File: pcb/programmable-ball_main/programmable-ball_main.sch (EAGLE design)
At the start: 4 parts, among them J1 12402012E212A, U1 MDBT50Q-1MV2

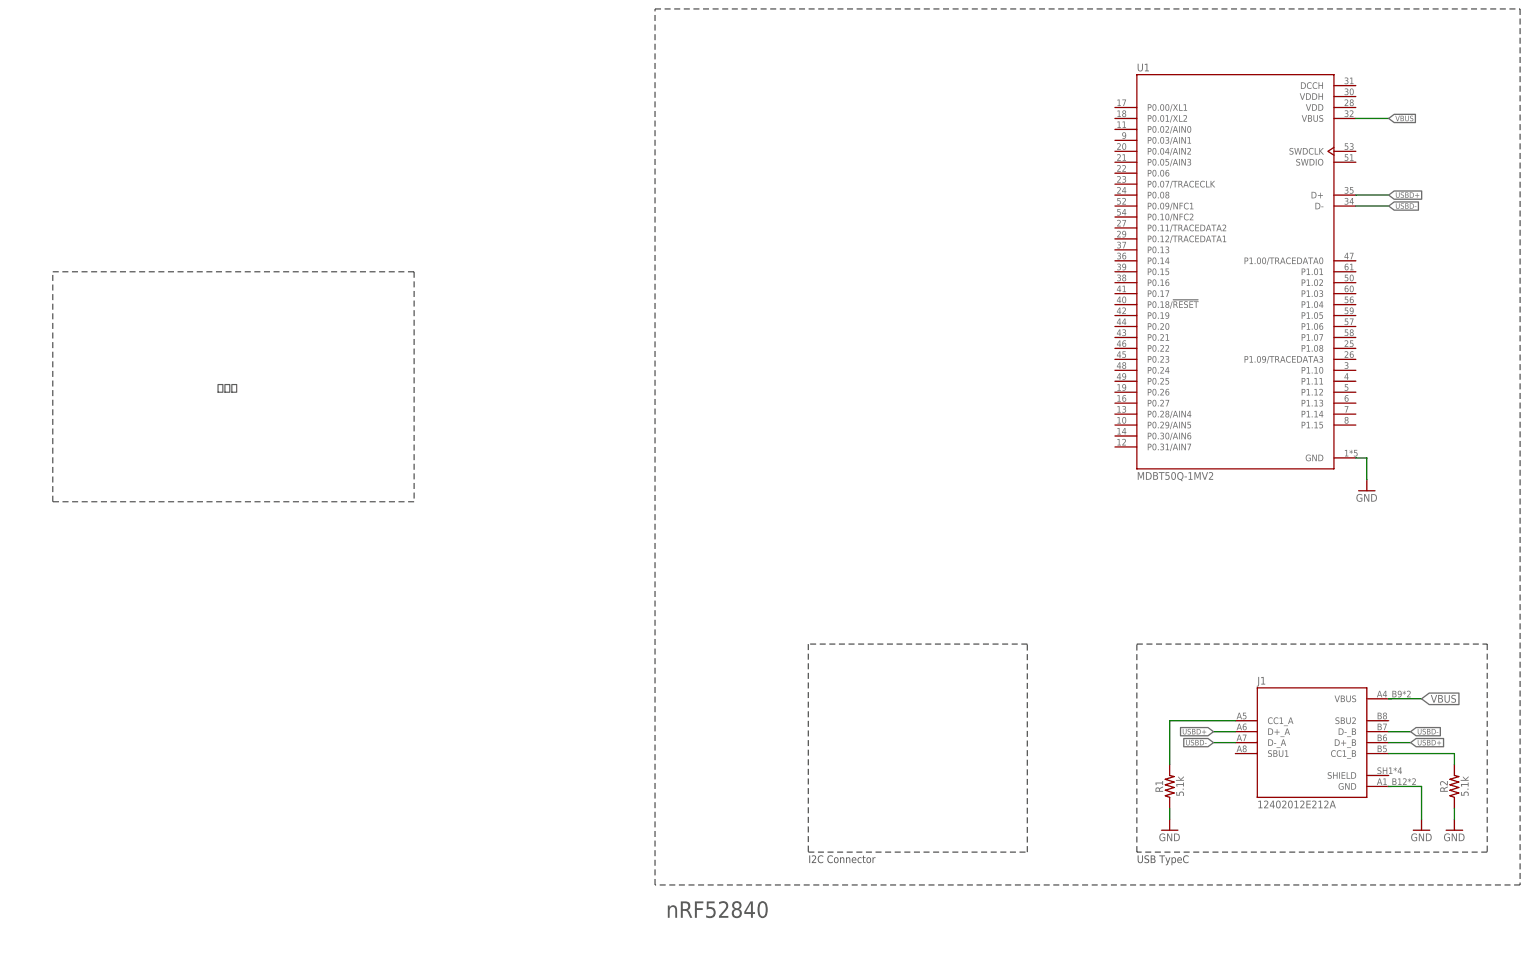
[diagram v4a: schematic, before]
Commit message: スイッチを追加 #4
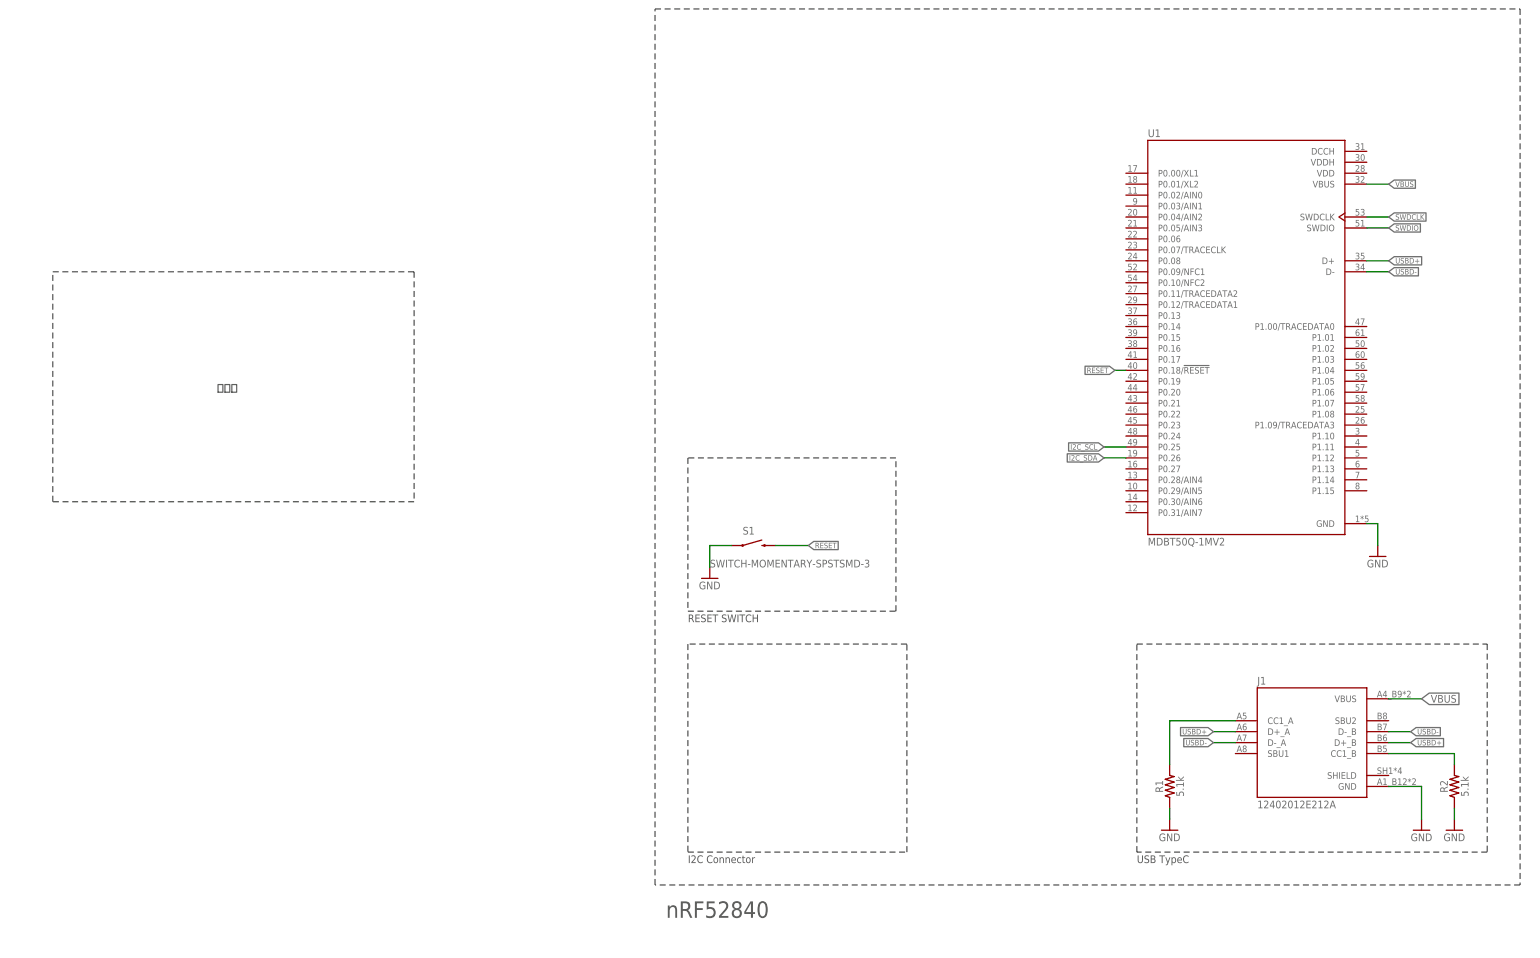
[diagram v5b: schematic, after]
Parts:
- added S1: SWITCH-MOMENTARY-SPSTSMD-3, SparkFun-Retired:SWITCH-MOMENTARY-SPSTSMD-3
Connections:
- new net I2C_SCL: U1.P0.25
- new net I2C_SDA: U1.P0.26
- new net RESET: S1.2, U1.P0.18/!RESET
- new net SWDCLK: U1.SWDCLK
- new net SWDIO: U1.SWDIO
- net GND: now also S1.1
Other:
- note added: "RESET SWITCH"
- moved on the sheet: U1
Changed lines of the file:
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@@
 <part name="R1" library="SparkFun-Resistors" deviceset="5.1KOHM" device="-0402T-1/16W-1%" value="5.1k"/>
 <part name="R2" library="SparkFun-Resistors" deviceset="5.1KOHM" device="-0402T-1/16W-1%" value="5.1k"/>
+<part name="S1" library="SparkFun-Retired" deviceset="SWITCH-MOMENTARY-SPST" device="SMD-3"/>
+<part name="GND5" library="supply1" library_urn="urn:adsk.eagle:library:371" deviceset="GND" device=""/>
 </parts>
 <sheets>
@@
 <wire x1="276.86" y1="50.8" x2="276.86" y2="99.06" width="0.1524" layer="97" style="shortdash"/>
 <text x="276.86" y="48.26" size="1.778" layer="97">USB TypeC</text>
-<wire x1="200.66" y1="99.06" x2="200.66" y2="50.8" width="0.1524" layer="97" style="shortdash"/>
-<wire x1="200.66" y1="50.8" x2="251.46" y2="50.8" width="0.1524" layer="97" style="shortdash"/>
-<wire x1="251.46" y1="50.8" x2="251.46" y2="99.06" width="0.1524" layer="97" style="shortdash"/>
-<wire x1="251.46" y1="99.06" x2="200.66" y2="99.06" width="0.1524" layer="97" style="shortdash"/>
-<text x="200.66" y="48.26" size="1.778" layer="97">I2C Connector</text>
+<wire x1="172.72" y1="99.06" x2="172.72" y2="50.8" width="0.1524" layer="97" style="shortdash"/>
+<wire x1="172.72" y1="50.8" x2="223.52" y2="50.8" width="0.1524" layer="97" style="shortdash"/>
+<wire x1="223.52" y1="50.8" x2="223.52" y2="99.06" width="0.1524" layer="97" style="shortdash"/>
+<wire x1="223.52" y1="99.06" x2="172.72" y2="99.06" width="0.1524" layer="97" style="shortdash"/>
+<text x="172.72" y="48.26" size="1.778" layer="97">I2C Connector</text>
+<wire x1="172.72" y1="142.24" x2="172.72" y2="106.68" width="0.1524" layer="97" style="shortdash"/>
+<wire x1="172.72" y1="106.68" x2="220.98" y2="106.68" width="0.1524" layer="97" style="shortdash"/>
+<wire x1="220.98" y1="106.68" x2="220.98" y2="142.24" width="0.1524" layer="97" style="shortdash"/>
+<wire x1="220.98" y1="142.24" x2="172.72" y2="142.24" width="0.1524" layer="97" style="shortdash"/>
+<text x="172.72" y="104.14" size="1.778" layer="97">RESET SWITCH</text>
 </plain>
 <instances>
@@
 <attribute name="SHEET" x="368.3" y="4.445" size="2.54" layer="94" font="vector"/>
 </instance>
-<instance part="U1" gate="G$1" x="299.72" y="185.42" smashed="yes">
-<attribute name="NAME" x="276.86" y="231.902" size="1.778" layer="95"/>
-<attribute name="VALUE" x="276.86" y="137.16" size="1.778" layer="96"/>
-</instance>
-<instance part="GND1" gate="1" x="330.2" y="134.62" smashed="yes">
-<attribute name="VALUE" x="327.66" y="132.08" size="1.778" layer="96"/>
+<instance part="U1" gate="G$1" x="302.26" y="170.18" smashed="yes">
+<attribute name="NAME" x="279.4" y="216.662" size="1.778" layer="95"/>
+<attribute name="VALUE" x="279.4" y="121.92" size="1.778" layer="96"/>
+</instance>
+<instance part="GND1" gate="1" x="332.74" y="119.38" smashed="yes">
+<attribute name="VALUE" x="330.2" y="116.84" size="1.778" layer="96"/>
 </instance>
 <instance part="GND3" gate="1" x="342.9" y="55.88" smashed="yes">
@@
 <attribute name="NAME" x="348.996" y="66.04" size="1.778" layer="95" font="vector" rot="R90" align="bottom-center"/>
 <attribute name="VALUE" x="352.044" y="66.04" size="1.778" layer="96" font="vector" rot="R90" align="top-center"/>
+</instance>
+<instance part="S1" gate="G$1" x="187.96" y="121.92" smashed="yes">
+<attribute name="NAME" x="185.42" y="124.46" size="1.778" layer="95"/>
+<attribute name="VALUE" x="177.8" y="116.84" size="1.778" layer="96"/>
+</instance>
+<instance part="GND5" gate="1" x="177.8" y="114.3" smashed="yes">
+<attribute name="VALUE" x="175.26" y="111.76" size="1.778" layer="96"/>
 </instance>
 </instances>
@@
 <pinref part="U1" gate="G$1" pin="GND"/>
 <pinref part="GND1" gate="1" pin="GND"/>
-<wire x1="327.66" y1="142.24" x2="330.2" y2="142.24" width="0.1524" layer="91"/>
-<wire x1="330.2" y1="142.24" x2="330.2" y2="137.16" width="0.1524" layer="91"/>
+<wire x1="330.2" y1="127" x2="332.74" y2="127" width="0.1524" layer="91"/>
+<wire x1="332.74" y1="127" x2="332.74" y2="121.92" width="0.1524" layer="91"/>
 </segment>
 <segment>
@@
 <wire x1="350.52" y1="60.96" x2="350.52" y2="58.42" width="0.1524" layer="91"/>
 </segment>
+<segment>
+<pinref part="GND5" gate="1" pin="GND"/>
+<wire x1="177.8" y1="116.84" x2="177.8" y2="121.92" width="0.1524" layer="91"/>
+<pinref part="S1" gate="G$1" pin="1"/>
+<wire x1="177.8" y1="121.92" x2="182.88" y2="121.92" width="0.1524" layer="91"/>
+</segment>
 </net>
 <net name="VBUS" class="0">
 <segment>
 <pinref part="U1" gate="G$1" pin="VBUS"/>
-<wire x1="327.66" y1="220.98" x2="335.28" y2="220.98" width="0.1524" layer="91"/>
-<label x="335.28" y="220.98" size="1.27" layer="95" xref="yes"/>
+<wire x1="330.2" y1="205.74" x2="335.28" y2="205.74" width="0.1524" layer="91"/>
+<label x="335.28" y="205.74" size="1.27" layer="95" xref="yes"/>
 </segment>
 <segment>
@@
 <segment>
 <pinref part="U1" gate="G$1" pin="D+"/>
-<wire x1="327.66" y1="203.2" x2="335.28" y2="203.2" width="0.1524" layer="91"/>
-<label x="335.28" y="203.2" size="1.27" layer="95" xref="yes"/>
+<wire x1="330.2" y1="187.96" x2="335.28" y2="187.96" width="0.1524" layer="91"/>
+<label x="335.28" y="187.96" size="1.27" layer="95" xref="yes"/>
 </segment>
 <segment>
@@
 <segment>
 <pinref part="U1" gate="G$1" pin="D-"/>
-<wire x1="327.66" y1="200.66" x2="335.28" y2="200.66" width="0.1524" layer="91"/>
-<label x="335.28" y="200.66" size="1.27" layer="95" xref="yes"/>
+<wire x1="330.2" y1="185.42" x2="335.28" y2="185.42" width="0.1524" layer="91"/>
+<label x="335.28" y="185.42" size="1.27" layer="95" xref="yes"/>
 </segment>
 <segment>
@@
 </segment>
 </net>
+<net name="RESET" class="0">
+<segment>
+<pinref part="U1" gate="G$1" pin="P0.18/!RESET"/>
+<wire x1="274.32" y1="162.56" x2="271.78" y2="162.56" width="0.1524" layer="91"/>
+<label x="271.78" y="162.56" size="1.27" layer="95" rot="R180" xref="yes"/>
+</segment>
+<segment>
+<pinref part="S1" gate="G$1" pin="2"/>
+<wire x1="193.04" y1="121.92" x2="200.66" y2="121.92" width="0.1524" layer="91"/>
+<label x="200.66" y="121.92" size="1.27" layer="95" xref="yes"/>
+</segment>
+</net>
+<net name="I2C_SCL" class="0">
+<segment>
+<pinref part="U1" gate="G$1" pin="P0.25"/>
+<wire x1="274.32" y1="144.78" x2="269.24" y2="144.78" width="0.1524" layer="91"/>
+<label x="269.24" y="144.78" size="1.27" layer="95" rot="R180" xref="yes"/>
+</segment>
+</net>
+<net name="I2C_SDA" class="0">
+<segment>
+<pinref part="U1" gate="G$1" pin="P0.26"/>
+<wire x1="274.32" y1="142.24" x2="269.24" y2="142.24" width="0.1524" layer="91"/>
+<label x="269.24" y="142.24" size="1.27" layer="95" rot="R180" xref="yes"/>
+</segment>
+</net>
+<net name="SWDCLK" class="0">
+<segment>
+<pinref part="U1" gate="G$1" pin="SWDCLK"/>
+<wire x1="330.2" y1="198.12" x2="335.28" y2="198.12" width="0.1524" layer="91"/>
+<label x="335.28" y="198.12" size="1.27" layer="95" xref="yes"/>
+</segment>
+</net>
+<net name="SWDIO" class="0">
+<segment>
+<pinref part="U1" gate="G$1" pin="SWDIO"/>
+<wire x1="330.2" y1="195.58" x2="335.28" y2="195.58" width="0.1524" layer="91"/>
+<label x="335.28" y="195.58" size="1.27" layer="95" xref="yes"/>
+</segment>
+</net>

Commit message: 3.3VのレギュレータとVBATよりVBUSを優先するように修正
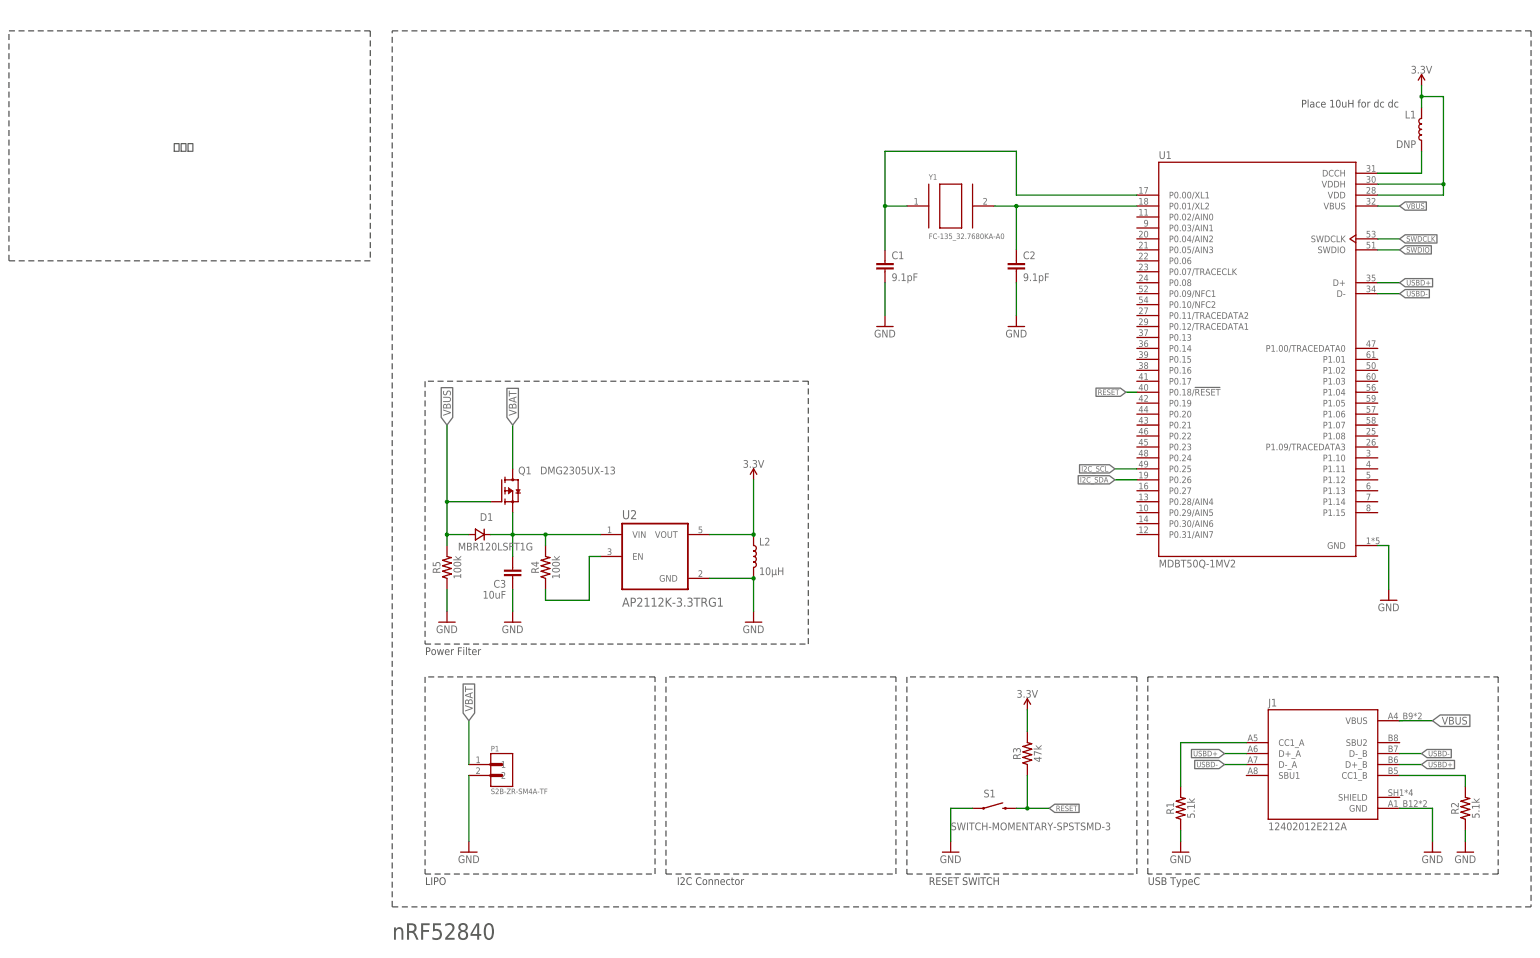
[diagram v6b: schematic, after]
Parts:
- added C1, C2: 9.1pF, SparkFun-Capacitors:9.1PF-0402-TIGHT
- added C3: 10uF, SparkFun-Capacitors:10UF-0402T-6.3V-20%
- added D1: MBR120LSFT1G, zetex:DSOD323
- added L1: DNP, SparkFun-Coils:10μH_SHIELDED_INDUCTOR0805
- added L2: 10μH, SparkFun-Coils:10μH_SHIELDED_INDUCTOR0805
- added P1: S2B-ZR-SM4A-TF, S2B-ZR-SM4A-TF:S2B-ZR-SM4A-TF
- added Q1: DMG2305UX-13, DMG2305UX-13:DMG2305UX-13
- added R3: 47k, SparkFun-Resistors:47KOHM-0402-1/10W-1%
- added R4, R5: 100k, SparkFun-Resistors:100KOHM-0402T-1/16W-1%
- added U2: AP2112K-3.3TRG1, AP2112K-3.3TRG1:AP2112K-3.3TRG1
- added Y1: FC-135_32.7680KA-A0, FC-135_32.7680KA-A0:FC-135_32.7680KA-A0
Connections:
- new net 3.3V: L1.1, L2.1, R3.2, U1.VDD, U1.VDDH, U2.VOUT
- new net N$3: C2.1, U1.P0.01/XL2, Y1.2
- new net N$4: C1.1, U1.P0.00/XL1, Y1.1
- new net N$5: L1.2, U1.DCCH
- new net N$6: C3.2, D1.C, Q1.S, R4.2, U2.VIN
- new net N$7: R4.1, U2.EN
- new net VBAT: P1.1, Q1.D
- net GND: now also C1.2, C2.2, C3.1, L2.2, P1.2, R5.1, U2.GND
- net RESET: now also R3.1
- net VBUS: now also D1.A, Q1.G, R5.2
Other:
- note added: "LIPO"
- note added: "Place 10uH for dc dc"
- note added: "Power Filter"
- moved on the sheet: J1, R1, R2, S1, U1

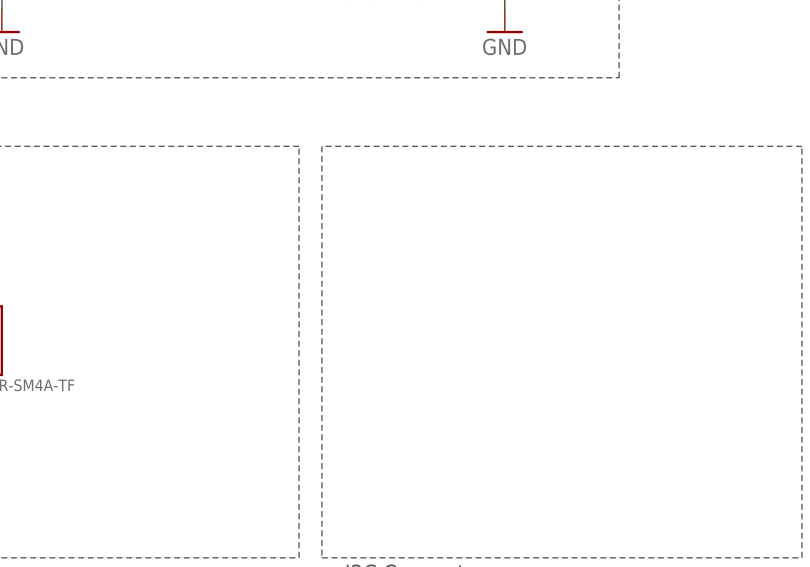
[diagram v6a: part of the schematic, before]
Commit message: スライドスイッチを追加 #4
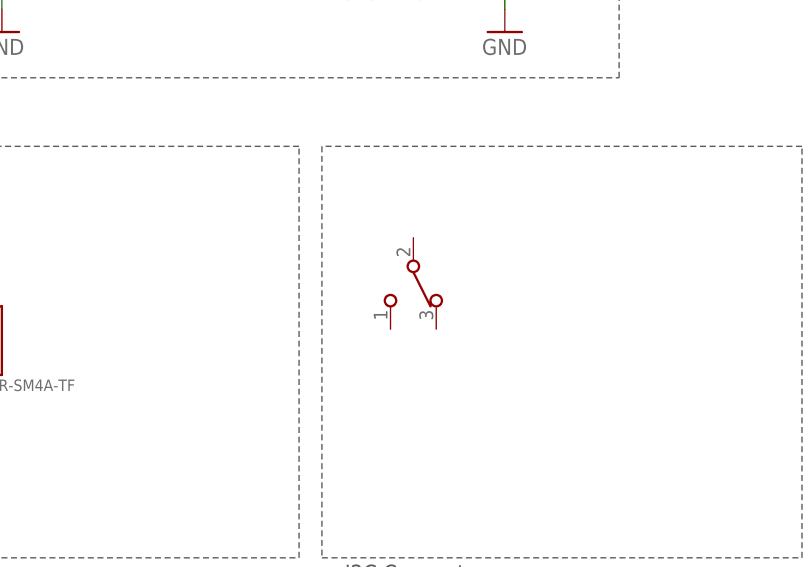
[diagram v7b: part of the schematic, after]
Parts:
- added SW1: CAS-120CAS-120B1, Switch:CAS-120CAS-120B1
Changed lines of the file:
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@@
 <part name="R5" library="SparkFun-Resistors" deviceset="100KOHM" device="-0402T-1/16W-1%" value="100k"/>
 <part name="C3" library="SparkFun-Capacitors" deviceset="10UF" device="-0402T-6.3V-20%" value="10uF"/>
+<part name="SW1" library="Switch" deviceset="CAS-120" device="CAS-120B1"/>
 </parts>
 <sheets>
@@
 <attribute name="VALUE" x="130.556" y="111.379" size="1.778" layer="96" font="vector" rot="R180"/>
 </instance>
+<instance part="SW1" gate="G$1" x="177.8" y="76.2" smashed="yes"/>
 </instances>
 <busses>
